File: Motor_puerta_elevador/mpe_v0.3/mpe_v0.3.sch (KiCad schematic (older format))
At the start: 34 parts, among them J1 IBT2, J10 ENCODER, J2 POWER, J3 MOTOR, J4 PROG, J5 IN1, J6 IN1, J7 IN1, J8 IN1, J9 IN1, P1 Power, P2 Analog, P3 Digital, P4 Digital, P5 CONN_01X01, P6 CONN_01X01, P7 CONN_01X01, P8 CONN_01X01, U1 ATmega3250PA-AU, U2 PC817, U3 PC817, U4 PC817, U5 PC817, U6 PC817

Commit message: ordenar pcb
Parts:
- added J11, J12: IN+, Connector_Pin:Pin_D1.0mm_L10.0mm, symbol Connector_Generic:Conn_01x01
- added J13, J14: IN-, Connector_Pin:Pin_D1.0mm_L10.0mm, symbol Connector_Generic:Conn_01x01
- added J15, J16: OUT+, Connector_Pin:Pin_D1.0mm_L10.0mm, symbol Connector_Generic:Conn_01x01
- added J17, J18: OUT-, Connector_Pin:Pin_D1.0mm_L10.0mm, symbol Connector_Generic:Conn_01x01
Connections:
- net +24V: now also J5.3 (Pin_3), J6.3 (Pin_3), J8.3 (Pin_3), J9.3 (Pin_3), J11.1 (Pin_1), J12.1 (Pin_1); no longer J5.1 (Pin_1), J6.1 (Pin_1), J8.1 (Pin_1), J9.1 (Pin_1)
- net +5V: now also J15.1 (Pin_1), J16.1 (Pin_1)
- net Earth: now also J5.1 (Pin_1), J6.1 (Pin_1), J8.1 (Pin_1), J9.1 (Pin_1), J13.1 (Pin_1), J14.1 (Pin_1); no longer J5.3 (Pin_3), J6.3 (Pin_3), J8.3 (Pin_3), J9.3 (Pin_3)
- net GND: now also J17.1 (Pin_1), J18.1 (Pin_1)
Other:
- note added: "DC-DC"
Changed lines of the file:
@@
 L power:Earth #PWR0102
 U 1 1 62C8B8C8
-P 1600 1950
-F 0 "#PWR0102" H 1600 1700 50  0001 C CNN
-F 1 "Earth" H 1600 1800 50  0001 C CNN
-F 2 "" H 1600 1950 50  0001 C CNN
-F 3 "~" H 1600 1950 50  0001 C CNN
-	1    1600 1950
+P 1350 1850
+F 0 "#PWR0102" H 1350 1600 50  0001 C CNN
+F 1 "Earth" H 1350 1700 50  0001 C CNN
+F 2 "" H 1350 1850 50  0001 C CNN
+F 3 "~" H 1350 1850 50  0001 C CNN
+	1    1350 1850
 	1    0    0    -1
 $EndComp
@@
 L power:+24V #PWR0106
 U 1 1 62CA08BC
-P 1650 1700
-F 0 "#PWR0106" H 1650 1550 50  0001 C CNN
-F 1 "+24V" H 1665 1873 50  0000 C CNN
-F 2 "" H 1650 1700 50  0001 C CNN
-F 3 "" H 1650 1700 50  0001 C CNN
-	1    1650 1700
+P 1350 1200
+F 0 "#PWR0106" H 1350 1050 50  0001 C CNN
+F 1 "+24V" H 1365 1373 50  0000 C CNN
+F 2 "" H 1350 1200 50  0001 C CNN
+F 3 "" H 1350 1200 50  0001 C CNN
+	1    1350 1200
 	1    0    0    -1
 $EndComp
@@
 F 3 "~" H 1350 4650 50  0001 C CNN
 	1    1350 4650
-	-1   0    0    -1
+	-1   0    0    1
 $EndComp
 $Comp
@@
 	1    0    0    -1
 $EndComp
-$Comp
-L Connector:Screw_Terminal_01x03 J6
-U 1 1 62DEB939
-P 1350 5200
-F 0 "J6" H 1500 5150 50  0000 C CNN
-F 1 "IN1" H 1500 5250 50  0000 C CNN
-F 2 "TerminalBlock:TerminalBlock_bornier-3_P5.08mm" H 1350 5200 50  0001 C CNN
-F 3 "~" H 1350 5200 50  0001 C CNN
-	1    1350 5200
-	-1   0    0    -1
-$EndComp
-Wire Wire Line
-	1550 4750 1600 4750
-Wire Wire Line
-	1550 5300 1600 5300
-Connection ~ 1600 5300
-Wire Wire Line
-	1600 5300 1600 5850
 $Comp
 L Connector:Screw_Terminal_01x03 J7
@@
 F 3 "~" H 1350 6300 50  0001 C CNN
 	1    1350 6300
-	-1   0    0    -1
+	-1   0    0    1
 $EndComp
 $Comp
@@
 F 3 "~" H 1350 6850 50  0001 C CNN
 	1    1350 6850
-	-1   0    0    -1
-$EndComp
-Wire Wire Line
-	1550 4550 1700 4550
-Wire Wire Line
-	1700 4550 1700 4400
+	-1   0    0    1
+$EndComp
 Wire Wire Line
 	1550 4650 1800 4650
@@
 Wire Wire Line
 	1800 4550 1850 4550
-Wire Wire Line
-	1550 5850 1600 5850
-Connection ~ 1600 5850
-Wire Wire Line
-	1600 5850 1600 6400
-Wire Wire Line
-	1550 6400 1600 6400
-Connection ~ 1600 6400
-Wire Wire Line
-	1600 6400 1600 6950
-Wire Wire Line
-	1550 6950 1600 6950
-Connection ~ 1600 6950
-Wire Wire Line
-	1600 6950 1600 7100
 $Comp
 L power:Earth #PWR0112
@@
 Wire Wire Line
 	2150 6950 2150 6400
-Wire Wire Line
-	1550 6750 1700 6750
-Wire Wire Line
-	1700 6750 1700 6200
-Connection ~ 1700 4550
-Wire Wire Line
-	1550 5100 1700 5100
-Connection ~ 1700 5100
-Wire Wire Line
-	1700 5100 1700 4550
-Wire Wire Line
-	1550 5650 1700 5650
-Connection ~ 1700 5650
-Wire Wire Line
-	1700 5650 1700 5100
-Wire Wire Line
-	1550 6200 1700 6200
-Connection ~ 1700 6200
-Wire Wire Line
-	1700 6200 1700 5650
 $Comp
 L Device:R_Small R3
@@
 Wire Wire Line
 	2050 6750 2200 6750
-Wire Wire Line
-	1600 4750 1600 5300
 $Comp
 L Device:R_Small R8
@@
 Wire Wire Line
 	2950 5400 2950 5350
+Wire Wire Line
+	1700 4400 1700 4550
+Wire Wire Line
+	1600 4750 1600 5300
+$Comp
+L Connector:Screw_Terminal_01x03 J6
+U 1 1 62DEB939
+P 1350 5200
+F 0 "J6" H 1500 5150 50  0000 C CNN
+F 1 "IN1" H 1500 5250 50  0000 C CNN
+F 2 "TerminalBlock:TerminalBlock_bornier-3_P5.08mm" H 1350 5200 50  0001 C CNN
+F 3 "~" H 1350 5200 50  0001 C CNN
+	1    1350 5200
+	-1   0    0    1
+$EndComp
+Wire Wire Line
+	1550 4550 1700 4550
+Connection ~ 1700 4550
+Wire Wire Line
+	1700 4550 1700 5100
+Wire Wire Line
+	1550 4750 1600 4750
+Wire Wire Line
+	1550 5100 1700 5100
+Connection ~ 1700 5100
+Wire Wire Line
+	1700 5100 1700 5650
+Wire Wire Line
+	1550 5300 1600 5300
+Connection ~ 1600 5300
+Wire Wire Line
+	1600 5300 1600 5850
+Wire Wire Line
+	1550 5650 1700 5650
+Connection ~ 1700 5650
+Wire Wire Line
+	1700 5650 1700 6200
+Wire Wire Line
+	1550 5850 1600 5850
+Connection ~ 1600 5850
+Wire Wire Line
+	1600 5850 1600 6400
+Wire Wire Line
+	1550 6200 1700 6200
+Connection ~ 1700 6200
+Wire Wire Line
+	1700 6200 1700 6750
+Wire Wire Line
+	1550 6400 1600 6400
+Connection ~ 1600 6400
+Wire Wire Line
+	1600 6400 1600 6950
+Wire Wire Line
+	1550 6750 1700 6750
+Wire Wire Line
+	1550 6950 1600 6950
+Connection ~ 1600 6950
+Wire Wire Line
+	1600 6950 1600 7100
+$Comp
+L Connector_Generic:Conn_01x01 J11
+U 1 1 62CA1F80
+P 1650 1250
+F 0 "J11" H 1850 1250 50  0000 L CNN
+F 1 "IN+" H 1700 1250 50  0000 L CNN
+F 2 "Connector_Pin:Pin_D1.0mm_L10.0mm" H 1650 1250 50  0001 C CNN
+F 3 "~" H 1650 1250 50  0001 C CNN
+	1    1650 1250
+	1    0    0    -1
+$EndComp
+$Comp
+L Connector_Generic:Conn_01x01 J14
+U 1 1 62CA2506
+P 1650 1800
+F 0 "J14" H 1850 1800 50  0000 L CNN
+F 1 "IN-" H 1700 1800 50  0000 L CNN
+F 2 "Connector_Pin:Pin_D1.0mm_L10.0mm" H 1650 1800 50  0001 C CNN
+F 3 "~" H 1650 1800 50  0001 C CNN
+	1    1650 1800
+	1    0    0    -1
+$EndComp
+$Comp
+L Connector_Generic:Conn_01x01 J15
+U 1 1 62CA27F3
+P 2500 1250
+F 0 "J15" H 2850 1250 50  0000 C CNN
+F 1 "OUT+" H 2650 1250 50  0000 C CNN
+F 2 "Connector_Pin:Pin_D1.0mm_L10.0mm" H 2500 1250 50  0001 C CNN
+F 3 "~" H 2500 1250 50  0001 C CNN
+	1    2500 1250
+	-1   0    0    1
+$EndComp
+$Comp
+L Connector_Generic:Conn_01x01 J18
+U 1 1 62CA2B2F
+P 2500 1800
+F 0 "J18" H 2850 1800 50  0000 C CNN
+F 1 "OUT-" H 2650 1800 50  0000 C CNN
+F 2 "Connector_Pin:Pin_D1.0mm_L10.0mm" H 2500 1800 50  0001 C CNN
+F 3 "~" H 2500 1800 50  0001 C CNN
+	1    2500 1800
+	-1   0    0    1
+$EndComp
+Wire Wire Line
+	1350 1200 1350 1250
+Wire Wire Line
+	1350 1250 1450 1250
+Wire Wire Line
+	1350 1850 1350 1800
+Wire Wire Line
+	1350 1800 1450 1800
+Wire Notes Line
+	1550 1150 2600 1150
+Wire Notes Line
+	2600 1150 2600 1900
+Wire Notes Line
+	2600 1900 1550 1900
+Wire Notes Line
+	1550 1150 1550 1900
+Text Notes 1950 1550 0    50   ~ 0
+DC-DC
+$Comp
+L Connector_Generic:Conn_01x01 J12
+U 1 1 62D0AAC3
+P 1650 1400
+F 0 "J12" H 1850 1400 50  0000 L CNN
+F 1 "IN+" H 1700 1400 50  0000 L CNN
+F 2 "Connector_Pin:Pin_D1.0mm_L10.0mm" H 1650 1400 50  0001 C CNN
+F 3 "~" H 1650 1400 50  0001 C CNN
+	1    1650 1400
+	1    0    0    -1
+$EndComp
+$Comp
+L Connector_Generic:Conn_01x01 J13
+U 1 1 62D18E9D
+P 1650 1650
+F 0 "J13" H 1850 1650 50  0000 L CNN
+F 1 "IN-" H 1700 1650 50  0000 L CNN
+F 2 "Connector_Pin:Pin_D1.0mm_L10.0mm" H 1650 1650 50  0001 C CNN
+F 3 "~" H 1650 1650 50  0001 C CNN
+	1    1650 1650
+	1    0    0    -1
+$EndComp
+Wire Wire Line
+	1450 1400 1350 1400
+Wire Wire Line
+	1350 1400 1350 1250
+Connection ~ 1350 1250
+Wire Wire Line
+	1450 1650 1350 1650
+Wire Wire Line
+	1350 1650 1350 1800
+Connection ~ 1350 1800
+$Comp
+L Connector_Generic:Conn_01x01 J16
+U 1 1 62D3FE52
+P 2500 1400
+F 0 "J16" H 2850 1400 50  0000 C CNN
+F 1 "OUT+" H 2650 1400 50  0000 C CNN
+F 2 "Connector_Pin:Pin_D1.0mm_L10.0mm" H 2500 1400 50  0001 C CNN
+F 3 "~" H 2500 1400 50  0001 C CNN
+	1    2500 1400
+	-1   0    0    1
+$EndComp
+$Comp
+L Connector_Generic:Conn_01x01 J17
+U 1 1 62D40146
+P 2500 1650
+F 0 "J17" H 2850 1650 50  0000 C CNN
+F 1 "OUT-" H 2650 1650 50  0000 C CNN
+F 2 "Connector_Pin:Pin_D1.0mm_L10.0mm" H 2500 1650 50  0001 C CNN
+F 3 "~" H 2500 1650 50  0001 C CNN
+	1    2500 1650
+	-1   0    0    1
+$EndComp
+$Comp
+L power:+5V #PWR0116
+U 1 1 62D84D17
+P 2800 1200
+F 0 "#PWR0116" H 2800 1050 50  0001 C CNN
+F 1 "+5V" H 2815 1373 50  0000 C CNN
+F 2 "" H 2800 1200 50  0001 C CNN
+F 3 "" H 2800 1200 50  0001 C CNN
+	1    2800 1200
+	1    0    0    -1
+$EndComp
+$Comp
+L power:GND #PWR0117
+U 1 1 62D85583
+P 2800 1850
+F 0 "#PWR0117" H 2800 1600 50  0001 C CNN
+F 1 "GND" H 2805 1677 50  0000 C CNN
+F 2 "" H 2800 1850 50  0001 C CNN
+F 3 "" H 2800 1850 50  0001 C CNN
+	1    2800 1850
+	1    0    0    -1
+$EndComp
+Wire Wire Line
+	2800 1200 2800 1250
+Wire Wire Line
+	2800 1400 2700 1400
+Wire Wire Line
+	2700 1250 2800 1250
+Connection ~ 2800 1250
+Wire Wire Line
+	2800 1250 2800 1400
+Wire Wire Line
+	2800 1850 2800 1800
+Wire Wire Line
+	2800 1650 2700 1650
+Wire Wire Line
+	2700 1800 2800 1800
+Connection ~ 2800 1800
+Wire Wire Line
+	2800 1800 2800 1650
 $EndSCHEMATC

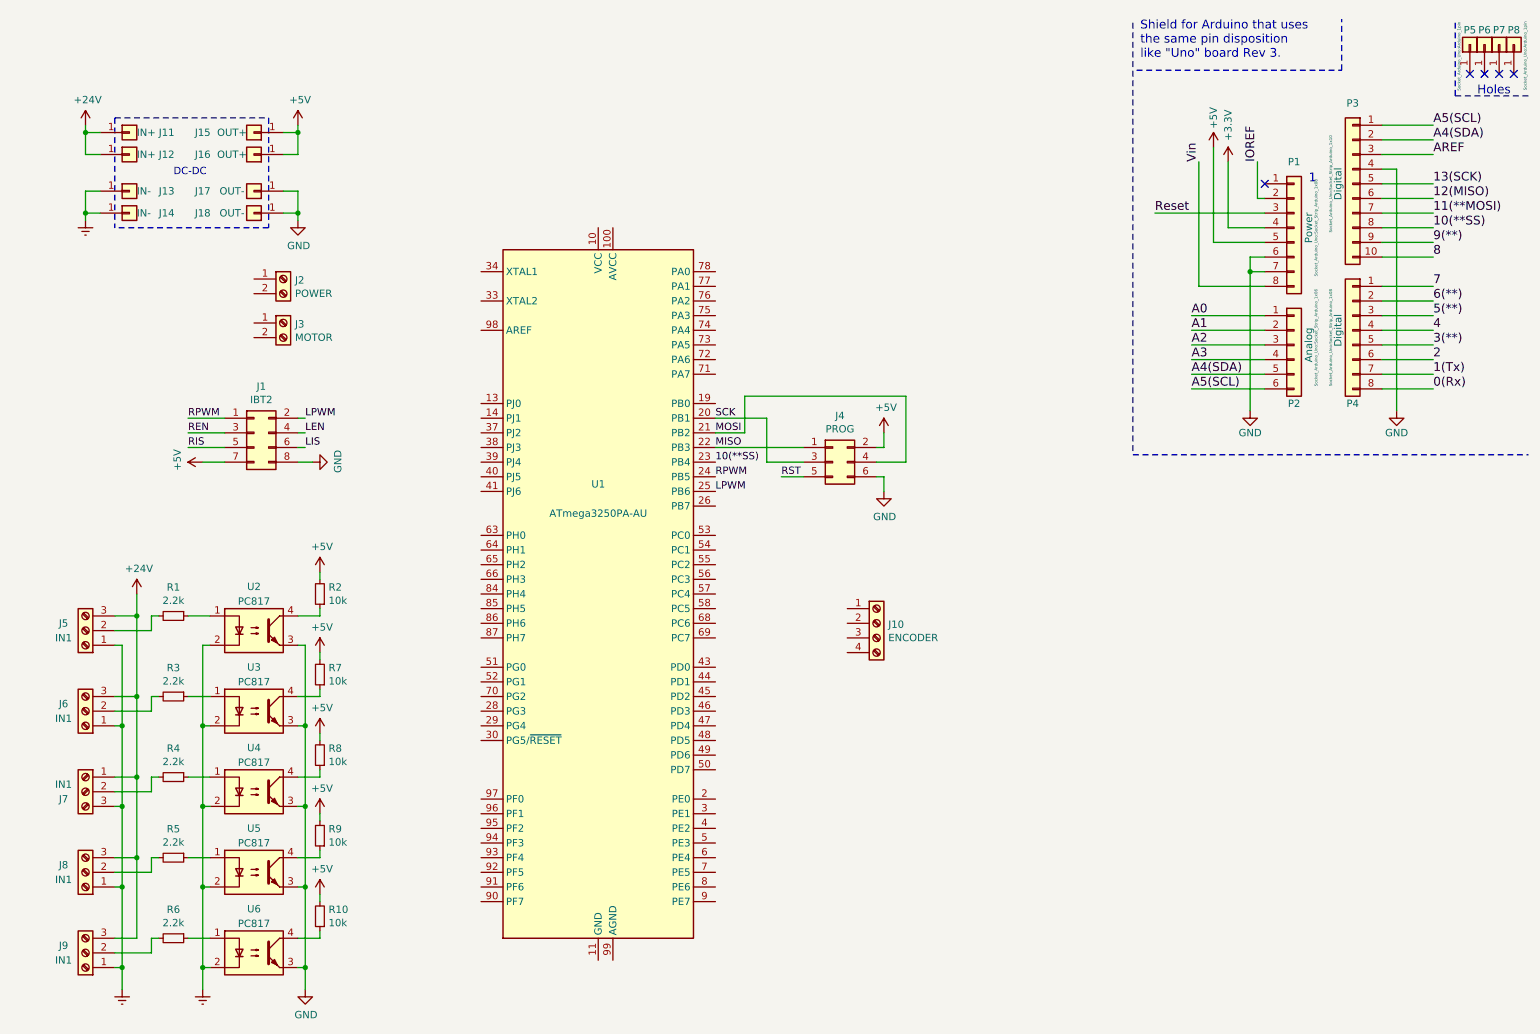
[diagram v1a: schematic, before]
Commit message: agregar librerías y primeras pistas PCB
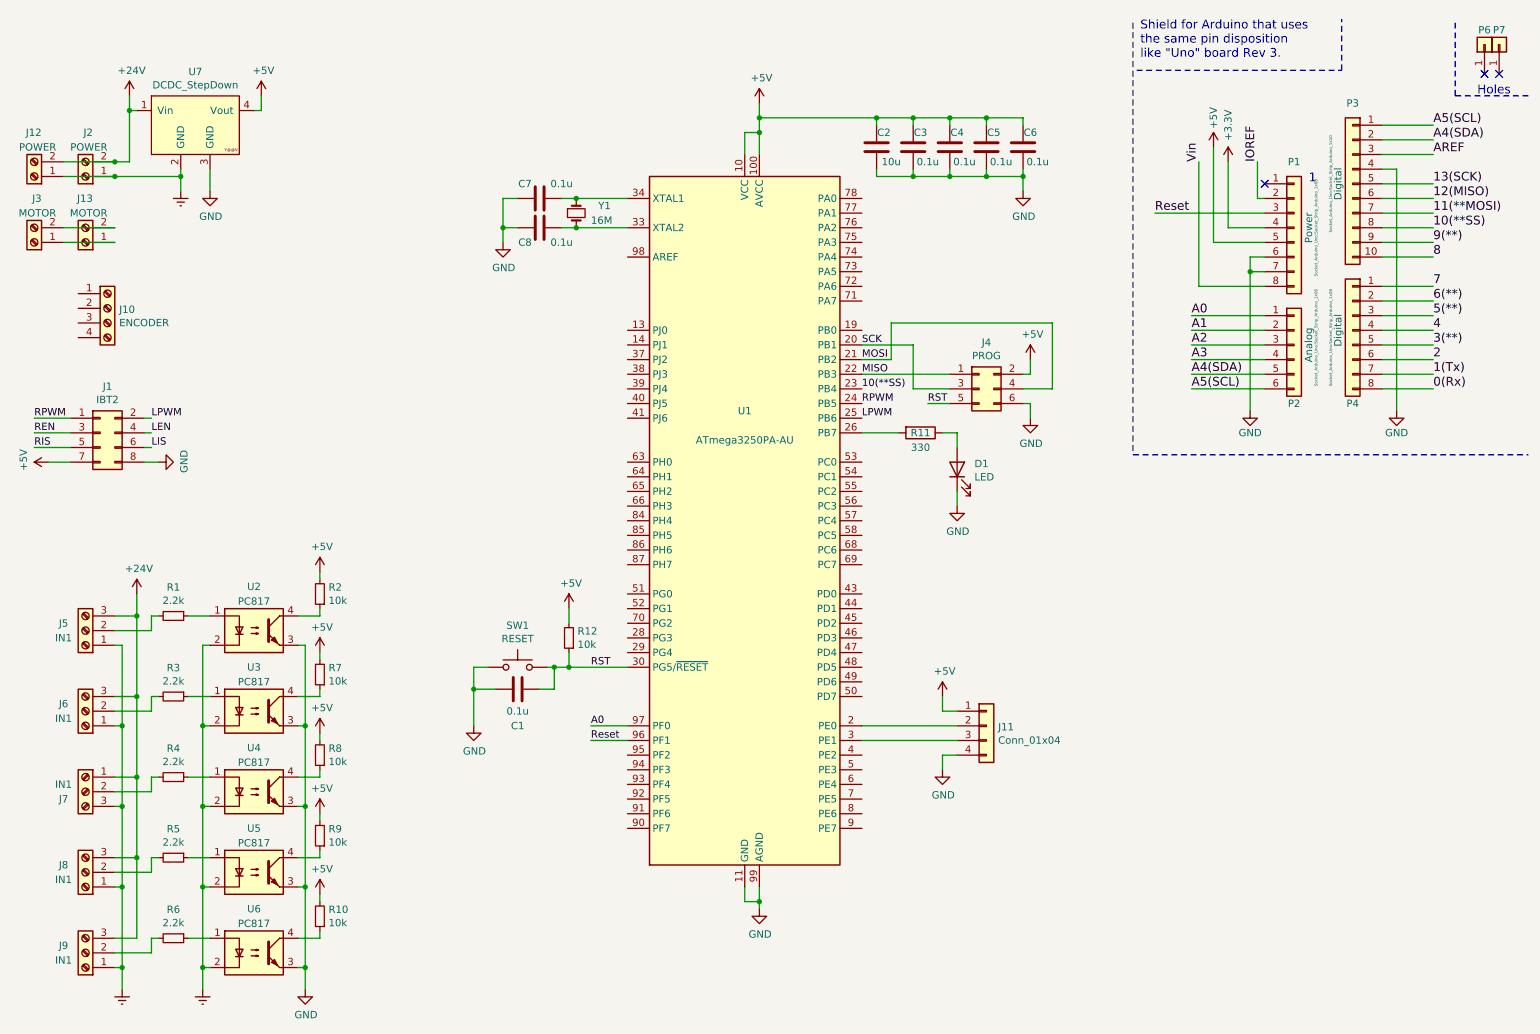
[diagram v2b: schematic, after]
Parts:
- removed J11, J12: IN+, Connector_Pin:Pin_D1.0mm_L10.0mm, symbol Connector_Generic:Conn_01x01
- removed J13, J14: IN-, Connector_Pin:Pin_D1.0mm_L10.0mm, symbol Connector_Generic:Conn_01x01
- removed J15, J16: OUT+, Connector_Pin:Pin_D1.0mm_L10.0mm, symbol Connector_Generic:Conn_01x01
- removed J17, J18: OUT-, Connector_Pin:Pin_D1.0mm_L10.0mm, symbol Connector_Generic:Conn_01x01
- removed P5, P8: CONN_01X01, Socket_Arduino_Uno:Arduino_1pin, symbol Connector_Generic:Conn_01x01
- added C1, C3, C4, C5, C6, C7, C8: 0.1u, Capacitor_SMD:C_0805_2012Metric_Pad1.18x1.45mm_HandSolder, symbol Device:C
- added C2: 10u, Capacitor_SMD:C_0805_2012Metric_Pad1.18x1.45mm_HandSolder, symbol Device:C
- added D1: LED, LED_THT:LED_D5.0mm, symbol Device:LED
- added J11: Conn_01x04, Connector_PinHeader_2.54mm:PinHeader_1x04_P2.54mm_Vertical, symbol Connector_Generic:Conn_01x04
- added J12: POWER, TerminalBlock:TerminalBlock_bornier-2_P5.08mm, symbol Connector:Screw_Terminal_01x02
- added J13: MOTOR, TerminalBlock:TerminalBlock_bornier-2_P5.08mm, symbol Connector:Screw_Terminal_01x02
- added R11: 330, Resistor_SMD:R_0805_2012Metric_Pad1.20x1.40mm_HandSolder, symbol Device:R
- added R12: 10k, Resistor_SMD:R_0805_2012Metric_Pad1.20x1.40mm_HandSolder, symbol Device:R_Small
- added SW1: RESET, Button_Switch_THT:SW_PUSH_6mm, symbol Switch:SW_Push
- added U7: DCDC_StepDown, LM2596:YAAJ_DCDC_StepDown_LM2596, symbol yaaj_dcdc_stepdown_lm2596:YAAJ_DCDC_StepDown_LM2596
- added Y1: 16M, Crystal:Crystal_HC49-4H_Vertical, symbol Device:Crystal_Small
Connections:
- net +24V: now also J2.2 (Pin_2), J12.2 (Pin_2), U7.1 (Vin)
- net +5V: now also U1.10 (VCC), U1.100 (AVCC), U1.31 (VCC), U1.80 (VCC), C2.2, C3.2, C4.2, C5.2, C6.2, J11.1 (Pin_1), R12.2, U7.4 (Vout)
- net A0: now also U1.97 (PF0)
- net Earth: now also J2.1 (Pin_1), J12.1 (Pin_1), U7.2 (GND)
- net GND: now also U1.11 (GND), U1.32 (GND), U1.81 (GND), U1.99 (AGND), C1.2, C2.1, C3.1, C4.1, C5.1, C6.1, C7.2, C8.2, D1.1 (K), J11.4 (Pin_4), SW1.1, U7.3 (GND)
- net RST: now also U1.30 (PG5/~RESET), C1.1, R12.1, SW1.2
- net Reset: now also U1.96 (PF1)
- net at U1.2 (PE0): now also J11.2 (Pin_2)
- net at U1.26 (PB7): now also R11.2
- net at U1.3 (PE1): now also J11.3 (Pin_3)
- net at U1.33 (XTAL2): now also C8.1, Y1.2
- net at U1.34 (XTAL1): now also C7.1, Y1.1
- net at J3.1 (Pin_1): now also J13.1 (Pin_1)
- net at J3.2 (Pin_2): now also J13.2 (Pin_2)
- new net: D1.2 (A), R11.1
- no-connect marks 5 -> 3
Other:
- note removed: "DC-DC"
- moved on the sheet: J1, J10, J2, J3, J4, U1
